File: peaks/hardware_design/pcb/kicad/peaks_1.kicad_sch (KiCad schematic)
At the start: 48 parts, among them IC3 DAC8552, J1 PJ301_THONKICONN6, J2 PJ301_THONKICONN6, Q1 8MHz, Q2 MMBT3904, Q3 MMBT3904, SW1 TAC_SWITCHPTH, SW2 TAC_SWITCHPTH, SW3 EVQQ2, SW4 LP4OA1PBCT, SW5 EVQQ2, SW6 LP4OA1PBCT

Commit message: peaks: smd boot + reset buttons
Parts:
- SW3, SW5: footprint peaks:EVQ-Q2 -> Library:k2-1808 pushbutton switch

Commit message: peaks: led/button footprint change
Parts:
- removed SW4, SW6: LP4OA1PBCT, peaks:LP4OA1PBCT, symbol peaks-eagle-import:LP4OA1PBCT
- added SW7, SW8: SW_Push_LED, Library:C&K_D6R, symbol Switch:SW_Push_LED
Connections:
- net GND: now also SW7.1, SW7.2, SW8.1, SW8.2
- net SW_TRIG_1: now also SW7.4
- net SW_TRIG_2: now also SW8.4
- net LED_TRIG_2: now reaches R10.1
- net LED_TRIG_2: now also SW8.3
- net LED_TRIG_1: now reaches R23.1
- net LED_TRIG_1: now also SW7.3

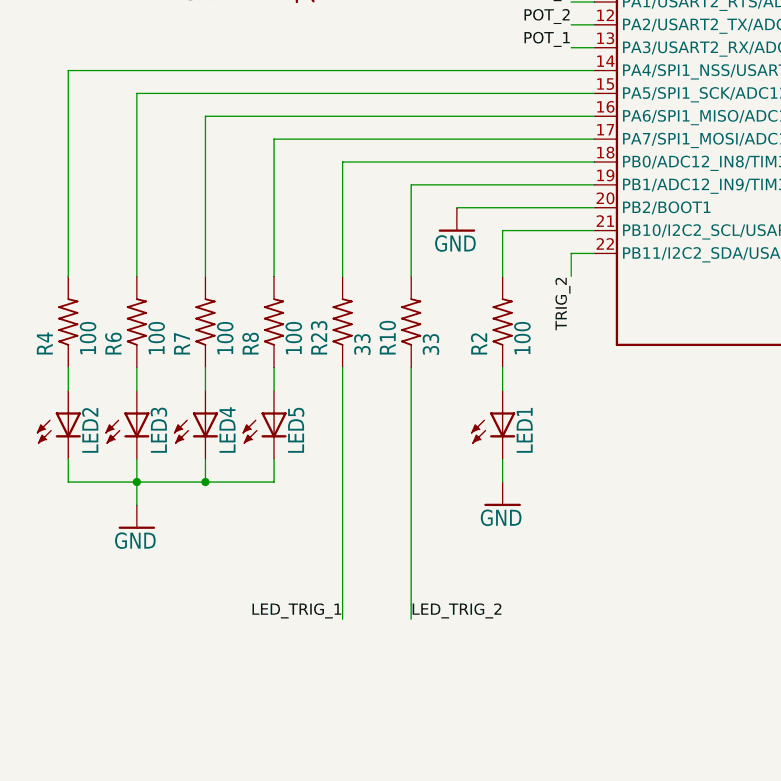
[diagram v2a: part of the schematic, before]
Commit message: peaks: change led resistor from 33 to 680 ohms
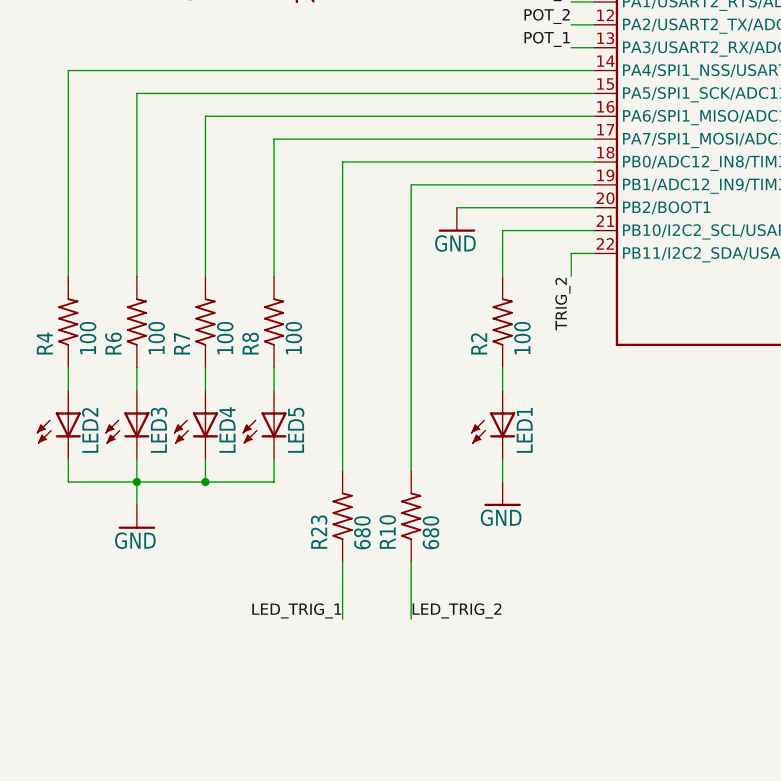
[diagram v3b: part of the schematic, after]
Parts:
- R10, R23: value 33 -> 680
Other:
- moved on the sheet: R10, R23
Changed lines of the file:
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@@
     (stroke (width 0.1524) (type solid))
   )
-  (wire (pts (xy 114.3 91.44) (xy 114.3 104.14))
+  (wire (pts (xy 114.3 91.44) (xy 114.3 125.73))
     (stroke (width 0.1524) (type solid))
   )
@@
     (stroke (width 0.1524) (type solid))
   )
-  (wire (pts (xy 121.92 114.3) (xy 121.92 142.24))
+  (wire (pts (xy 121.92 135.89) (xy 121.92 142.24))
     (stroke (width 0.1524) (type solid))
   )
@@
     (stroke (width 0.1524) (type solid))
   )
-  (wire (pts (xy 121.92 93.98) (xy 121.92 104.14))
+  (wire (pts (xy 121.92 93.98) (xy 121.92 125.73))
     (stroke (width 0.1524) (type solid))
   )
@@
     (stroke (width 0.1524) (type solid))
   )
-  (wire (pts (xy 114.3 114.3) (xy 114.3 142.24))
+  (wire (pts (xy 114.3 135.89) (xy 114.3 142.24))
     (stroke (width 0.1524) (type solid))
   )
@@
     )
   )
-  (symbol (lib_id "peaks-eagle-import:R-US_R0603") (at 121.92 109.22 90) (unit 1)
-    (in_bom yes) (on_board yes) (dnp no)
-    (property "Reference" "R10" (at 120.4214 113.03 0)
-      (effects (font (size 1.778 1.5113)) (justify left bottom))
-    )
-    (property "Value" "33" (at 125.222 113.03 0)
-      (effects (font (size 1.778 1.5113)) (justify left bottom))
-    )
-    (property "Footprint" "peaks:R0603" (at 121.92 109.22 0)
-      (effects (font (size 1.27 1.27)) hide)
-    )
-    (property "Datasheet" "" (at 121.92 109.22 0)
+  (symbol (lib_id "peaks-eagle-import:R-US_R0603") (at 121.92 130.81 90) (unit 1)
+    (in_bom yes) (on_board yes) (dnp no)
+    (property "Reference" "R10" (at 120.4214 134.62 0)
+      (effects (font (size 1.778 1.5113)) (justify left bottom))
+    )
+    (property "Value" "680" (at 125.222 134.62 0)
+      (effects (font (size 1.778 1.5113)) (justify left bottom))
+    )
+    (property "Footprint" "peaks:R0603" (at 121.92 130.81 0)
+      (effects (font (size 1.27 1.27)) hide)
+    )
+    (property "Datasheet" "" (at 121.92 130.81 0)
       (effects (font (size 1.27 1.27)) hide)
     )
@@
     )
   )
-  (symbol (lib_id "peaks-eagle-import:R-US_R0603") (at 114.3 109.22 90) (unit 1)
-    (in_bom yes) (on_board yes) (dnp no)
-    (property "Reference" "R23" (at 112.8014 113.03 0)
-      (effects (font (size 1.778 1.5113)) (justify left bottom))
-    )
-    (property "Value" "33" (at 117.602 113.03 0)
-      (effects (font (size 1.778 1.5113)) (justify left bottom))
-    )
-    (property "Footprint" "peaks:R0603" (at 114.3 109.22 0)
-      (effects (font (size 1.27 1.27)) hide)
-    )
-    (property "Datasheet" "" (at 114.3 109.22 0)
-      (effects (font (size 1.27 1.27)) hide)
-    )
+  (symbol (lib_id "peaks-eagle-import:R-US_R0603") (at 114.3 130.81 90) (unit 1)
+    (in_bom yes) (on_board yes) (dnp no)
+    (property "Reference" "R23" (at 112.8014 134.62 0)
+      (effects (font (size 1.778 1.5113)) (justify left bottom))
+    )
+    (property "Value" "680" (at 117.602 134.62 0)
+      (effects (font (size 1.778 1.5113)) (justify left bottom))
+    )
+    (property "Footprint" "peaks:R0603" (at 114.3 130.81 0)
+      (effects (font (size 1.27 1.27)) hide)
+    )
+    (property "Datasheet" "" (at 114.3 130.81 0)
+      (effects (font (size 1.27 1.27)) hide)
+    )
